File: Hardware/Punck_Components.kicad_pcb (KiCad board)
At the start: 2 copper layers, 91.3 x 100 mm, 109 parts, among them J1 Conn_01x12_Female, J2 Conn_01x12_Female, J3 Conn_01x12_Female, J4 Conn_01x12_Female, J5 SWD_Header, J6 USB_B_Micro, J7 Eurorack_10_pin_power, Q1 MMBT3904, Q2 MMBT3904, Q3 MMBT3904, Q4 MMBT3904, Q5 MMBT3904, Q6 MMBT3904, Q7 MMBT3904, U1 TL072, U2 STM32H743ZITx, U3 W25Q128JVS, U4 PCM5100APW, U5 LM2675M-5, U6 W25Q128JVS, U7 LD1117-3.3-4Tab, Y1 8MHz 20pF

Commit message: Component PCB Signal routing first draft
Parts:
- removed the C31 at (-24.4, 161.0)
- removed the C33 at (-33.0, 166.0)
- removed the C35 at (176.8, 56.9)
- removed the D2 at (168.4, 62.9)
- removed J6: USB_B_Micro, Custom_Footprints:USB_Micro-B_Amphenol
- removed TP10, TP11, TP12, TP9: TestPoint, TestPoint:TestPoint_Pad_2.0x2.0mm
- added C1: 4.7uF, Capacitor_SMD:C_0603_1608Metric_Pad1.08x0.95mm_HandSolder, F.Cu at (121.8, 81.0)
- added C15: 1uF, Capacitor_SMD:C_0603_1608Metric_Pad1.08x0.95mm_HandSolder, F.Cu at (107.8, 81.0)
- added C18: 1uF, Capacitor_SMD:C_0603_1608Metric_Pad1.08x0.95mm_HandSolder, F.Cu at (104.6, 81.0)
- added C19: 100nF, Capacitor_SMD:C_0603_1608Metric_Pad1.08x0.95mm_HandSolder, F.Cu at (106.2, 81.0)
- added C36: 10uF, Resistor_SMD:R_0805_2012Metric, F.Cu at (140.1, 58.0)
- added C37: 10uF, Resistor_SMD:R_0805_2012Metric, F.Cu at (137.7, 58.0)
- added R30: 33k, Resistor_SMD:R_0603_1608Metric_Pad0.98x0.95mm_HandSolder, F.Cu at (150.9, 58.6)
- added R31: 10k, Resistor_SMD:R_0603_1608Metric_Pad0.98x0.95mm_HandSolder, F.Cu at (148.9, 58.6)
- added R5: 100k, Resistor_SMD:R_0603_1608Metric, F.Cu at (130.0, 88.6)
- C34: value 22uF -> 100nF; footprint Capacitor_SMD:C_1210_3225Metric -> Resistor_SMD:R_0805_2012Metric
- C39: footprint Capacitor_SMD:CP_Elec_5x5.8 -> Resistor_SMD:R_1206_3216Metric
- L1: value 68uH -> 3.3uH; footprint Custom_Footprints:TDK_Inductor_6.9x7.2 -> Custom_Footprints:L_0806
- Q1, Q2, Q3, Q4, Q5, Q6, Q7: footprint Package_TO_SOT_THT:TO-92_Inline -> Package_TO_SOT_SMD:SOT-23
- U5: value LM2675M-5 -> TPS561201; footprint Package_SO:SOIC-8_3.9x4.9mm_P1.27mm -> Package_TO_SOT_SMD:SOT-23-6_Handsoldering
- Y1: footprint Crystal:Crystal_SMD_5032-2Pin_5.0x3.2mm_HandSoldering -> Crystal:Crystal_SMD_5032-2Pin_5.0x3.2mm
- moved J4 223.6 mm to (159.0, 112.0)
- moved J3 216.8 mm to (159.0, 56.0)
- moved Q4 197.3 mm to (145.6, 80.6), turned to 180 degrees
- moved R4 196.3 mm to (149.6, 70.6), turned to 180 degrees
- moved R27 195.7 mm to (152.6, 132.3), turned to 180 degrees
- moved J5 189.4 mm to (159.0, 101.8), turned to 90 degrees
- moved R29 188.4 mm to (149.6, 98.8), turned to 180 degrees
- moved Q6 188.2 mm to (145.6, 89.2), turned to 180 degrees
- moved Q2 187.3 mm to (145.6, 71.6), turned to 180 degrees
- moved TP8 186.6 mm to (109.4, 124.4)
- moved R10 185.7 mm to (149.8, 86.0)
- moved R2 184.7 mm to (149.6, 72.8)
- moved R6 183.6 mm to (149.6, 77.2)
- moved C11 182.6 mm to (130.0, 93.0), turned to 180 degrees
- moved Q5 182.0 mm to (145.6, 85.1), turned to 180 degrees
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- renumbered C19 to C20, C1 to C22, C15 to C23, C18 to C24, C20 to C25, C22 to C26, C23 to C27, C24 to C28, C25 to C29, C26 to C30, C27 to C31, C28 to C32, C29 to C33, C30 to C35, C32 to C38, C36 to C40, C37 to C41, C38 to C42, C40 to C44, D3 to D2, R17 to R10, R18 to R11, R3 to R12, R6 to R13, R7 to R14, R19 to R15, R8 to R16, R20 to R17, R21 to R18, R22 to R19, R11 to R20, R23 to R21, R14 to R22, R15 to R23, R16 to R25, R25 to R26, R26 to R27, R27 to R28, R28 to R29, R4 to R3, R5 to R4, R9 to R6, R10 to R7, R12 to R8, R13 to R9
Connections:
- C34 pad 1: VCC -> /VSW
- C34 pad 2: GND -> /CB
- J1 pad 1: +3.3VA -> GND
- J1 pad 10: /SA_LED -> /SAMPLER_A_VOL_POT
- J1 pad 11: /SNARE_IN -> /SAMPLER_B_VOICE_POT
- J1 pad 12: GND -> /HIHAT_DECAY_POT
- J1 pad 2: /KICK_IN -> /SAMPLER_A_VOICE_POT
- J1 pad 3: /SN_BTN -> /SAMPLER_A_SPEED_POT
- J1 pad 4: /SN_LED -> /KICK_ATTACK_POT
- J1 pad 5: /OH_BTN -> /KICK_DECAY_POT
- J1 pad 6: /OH_LED -> /KICK_VOL_POT
- J1 pad 7: /CH_BTN -> /SNARE_FILTER_POT
- J1 pad 8: /CH_LED -> /SNARE_TUNING_POT
- J1 pad 9: /SA_BTN -> /SNARE_VOL_POT
- J2 pad 1: /KI_BTN -> /HIHAT_VOL_POT
- J2 pad 10: /SNARE_TUNING_POT -> /CH_BTN
- J2 pad 11: /SNARE_VOL_POT -> /KI_BTN
- J2 pad 2: /KI_LED -> /SAMPLER_B_SPEED_POT
- J2 pad 3: /CH_IN -> /SAMPLER_B_VOL_POT
- J2 pad 4: /SB_BTN -> /TEMPO_POT
- J2 pad 5: /SB_LED -> /MIDI_LEARN
- J2 pad 6: /KICK_ATTACK_POT -> /SEQ_SELECT
- J2 pad 7: /KICK_DECAY_POT -> /SA_BTN
- J2 pad 8: /KICK_VOL_POT -> /SB_BTN
- J2 pad 9: /SNARE_FILTER_POT -> /SN_BTN
- J3 pad 1: /OH_IN -> GND
- J3 pad 10: /SAMPLER_B_VOL_POT -> /SA_LED
- J3 pad 11: /TEMPO_OUT -> /SB_LED
- J3 pad 12: GND -> +3.3VA
- J3 pad 2: /SAMPLERA_IN -> /KICK_IN
- J3 pad 3: /HIHAT_DECAY_POT -> /SAMPLER_A_IN
- J3 pad 4: /HIHAT_VOL_POT -> /SNARE_IN
- J3 pad 5: /SAMPLER_A_VOICE_POT -> /SAMPLER_B_IN
- J3 pad 6: /SAMPLER_A_SPEED_POT -> /CH_IN
- J3 pad 7: /SAMPLER_A_VOL_POT -> /MIDI_IN
- J3 pad 8: /SAMPLER_B_VOICE_POT -> /OH_IN
- J3 pad 9: /SAMPLER_B_SPEED_POT -> /TEMPO_OUT
- J4 pad 1: +3.3VA -> GND
- J4 pad 10: /AUDIO_OUT_R -> /AUDIO_OUT_L
- J4 pad 11: /AUDIO_OUT_L -> /AUDIO_OUT_R
- J4 pad 12: GND -> +3.3VA
- J4 pad 2: /SAMPLERB_IN -> /OH_BTN
- J4 pad 6: /MIDI_IN -> /KI_LED
- J4 pad 7: /MIDI_LEARN -> /SN_LED
- J4 pad 8: /SEQ_SELECT -> /CH_LED
- J4 pad 9: /TEMPO_POT -> /OH_LED
- L1 pad 2: +5V -> +3V3
- L2 pad 2: +3V3 -> /VO
- Q6 pad 3: /MIDI_RX -> /MIDI_CLAMP
- R15 pad 1: /MIDI_RX -> /MIDI_CLAMP
- U2 pad 1: /QSPI_IO2 -> /QSPI_BK1_IO2
- U2 pad 10: /KI_BTN -> unconnected-(U2-Pad10)
- U2 pad 11: /SN_BTN -> unconnected-(U2-Pad11)
- U2 pad 114: unconnected-(U2-Pad114) -> /OH_BTN
- U2 pad 12: /OH_BTN -> unconnected-(U2-Pad12)
- U2 pad 124: unconnected-(U2-Pad124) -> /OH_CLAMP
- U2 pad 125: /SAMPLER_A_CLAMP -> /MIDI_CLAMP
- U2 pad 128: /SAMPLER_B_CLAMP -> /CH_CLAMP
- U2 pad 13: /CH_BTN -> unconnected-(U2-Pad13)
- U2 pad 135: /SNARE_CLAMP -> /SAMPLER_B_CLAMP
- U2 pad 136: /CH_CLAMP -> /SNARE_CLAMP
- U2 pad 137: /KICK_CLAMP -> /SAMPLER_A_CLAMP
- U2 pad 138: GND -> Net-(R5-Pad2)
- U2 pad 14: /SA_BTN -> unconnected-(U2-Pad14)
- U2 pad 140: /DAC_LRCLK -> unconnected-(U2-Pad140)
- U2 pad 141: /MIDI_RX -> /KICK_CLAMP
- U2 pad 15: /SB_BTN -> unconnected-(U2-Pad15)
- U2 pad 64: unconnected-(U2-Pad64) -> /MIDI_LEARN
- U2 pad 65: unconnected-(U2-Pad65) -> /SEQ_SELECT
- U2 pad 66: unconnected-(U2-Pad66) -> /SA_BTN
- U2 pad 67: /MIDI_LEARN -> /SB_BTN
- U2 pad 68: /SEQ_SELECT -> /SN_BTN
- U2 pad 69: unconnected-(U2-Pad69) -> /CH_BTN
- U2 pad 73: unconnected-(U2-Pad73) -> /DAC_LRCLK
- U2 pad 78: unconnected-(U2-Pad78) -> /KI_BTN
- U2 pad 93: /OH_CLAMP -> unconnected-(U2-Pad93)
- U2 pad 96: /KI_LED_OUT -> /OH_LED_OUT
- U2 pad 97: /SN_LED_OUT -> /CH_LED_OUT
- U2 pad 98: /CH_LED_OUT -> /SN_LED_OUT
- U2 pad 99: /OH_LED_OUT -> /KI_LED_OUT
- U5 pad 1: Net-(C31-Pad2) -> GND
- U5 pad 2: unconnected-(U5-Pad2) -> /VSW
- U5 pad 3: unconnected-(U5-Pad3) -> VCC
- U5 pad 4: +5V -> /FB
- U5 pad 5: unconnected-(U5-Pad5) -> VCC
- U5 pad 6: GND -> /CB
- U7 pad 2: +3V3 -> /VO
- U7 pad 3: +5V -> VCC
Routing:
- net +3V3: track 0.00 -> 70.9 mm
- net VCC: track 0.00 -> 67.8 mm
- net /KI_BTN: track 0.00 -> 52.1 mm
- net /SAMPLER_A_VOICE_POT: track 0.00 -> 51.4 mm, vias 0 -> 1
- net /QSPI_CLK: track 0.00 -> 51.1 mm, vias 0 -> 2
- net /SAMPLER_A_SPEED_POT: track 0.00 -> 49.5 mm, vias 0 -> 1
- net /SAMPLER_B_VOL_POT: track 0.00 -> 49.4 mm, vias 0 -> 2
- net /CH_BTN: track 0.00 -> 48.6 mm
- net /SAMPLER_B_SPEED_POT: track 0.00 -> 48.2 mm, vias 0 -> 2
- net /OH_LED_OUT: track 0.00 -> 47.2 mm
- net /SN_BTN: track 0.00 -> 46.7 mm
- net /CH_LED_OUT: track 0.00 -> 45.3 mm
- net /KICK_ATTACK_POT: track 0.00 -> 45.1 mm
- net /HIHAT_VOL_POT: track 0.00 -> 45.0 mm
- net /USB_VBUS: track 0.00 -> 45.0 mm
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- added copper zone on In1.Cu, net /VSW
- added copper zone on B.Cu, net GND
- added copper zone on F.Cu, net GND
- added copper zone on In2.Cu, net GND
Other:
- board size 91.3 x 100 mm -> 91.2 x 99.8 mm
- copper layers 2 -> 4

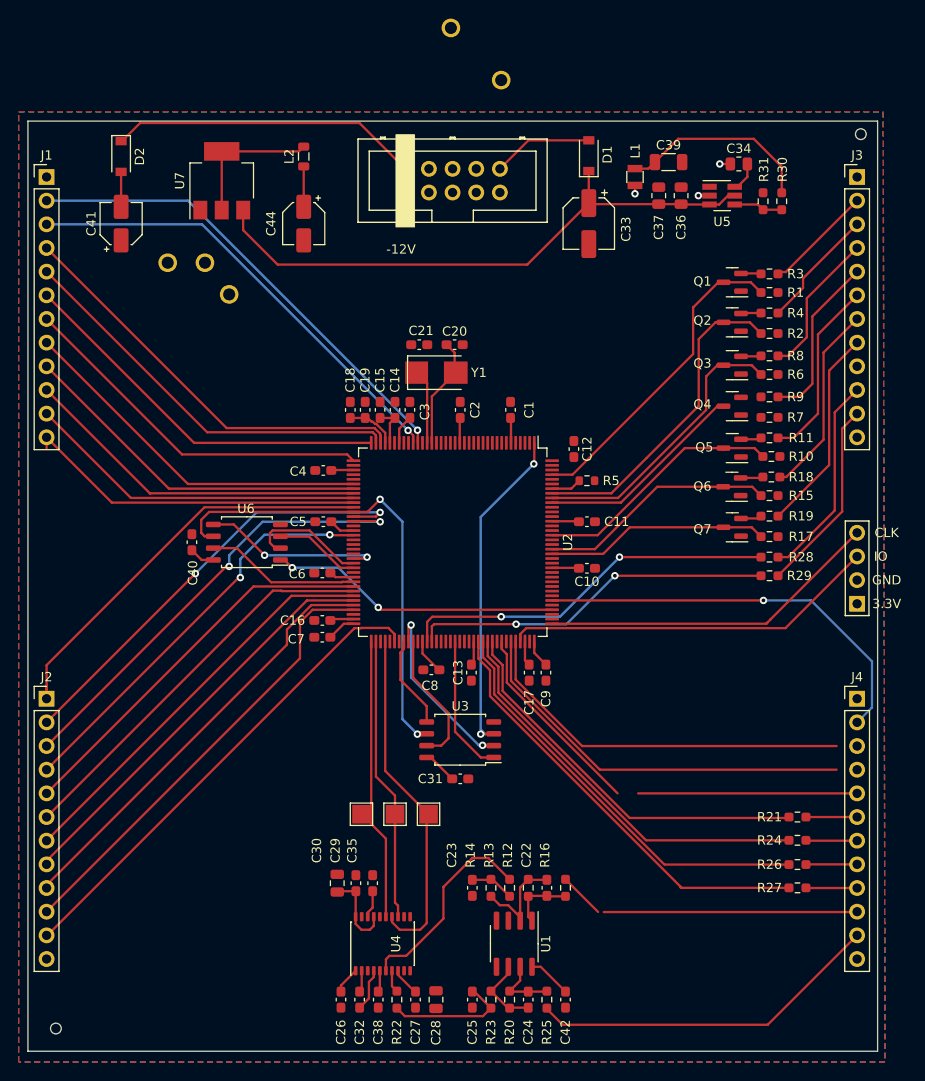
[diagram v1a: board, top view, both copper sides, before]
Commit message: Power routing on component PCB
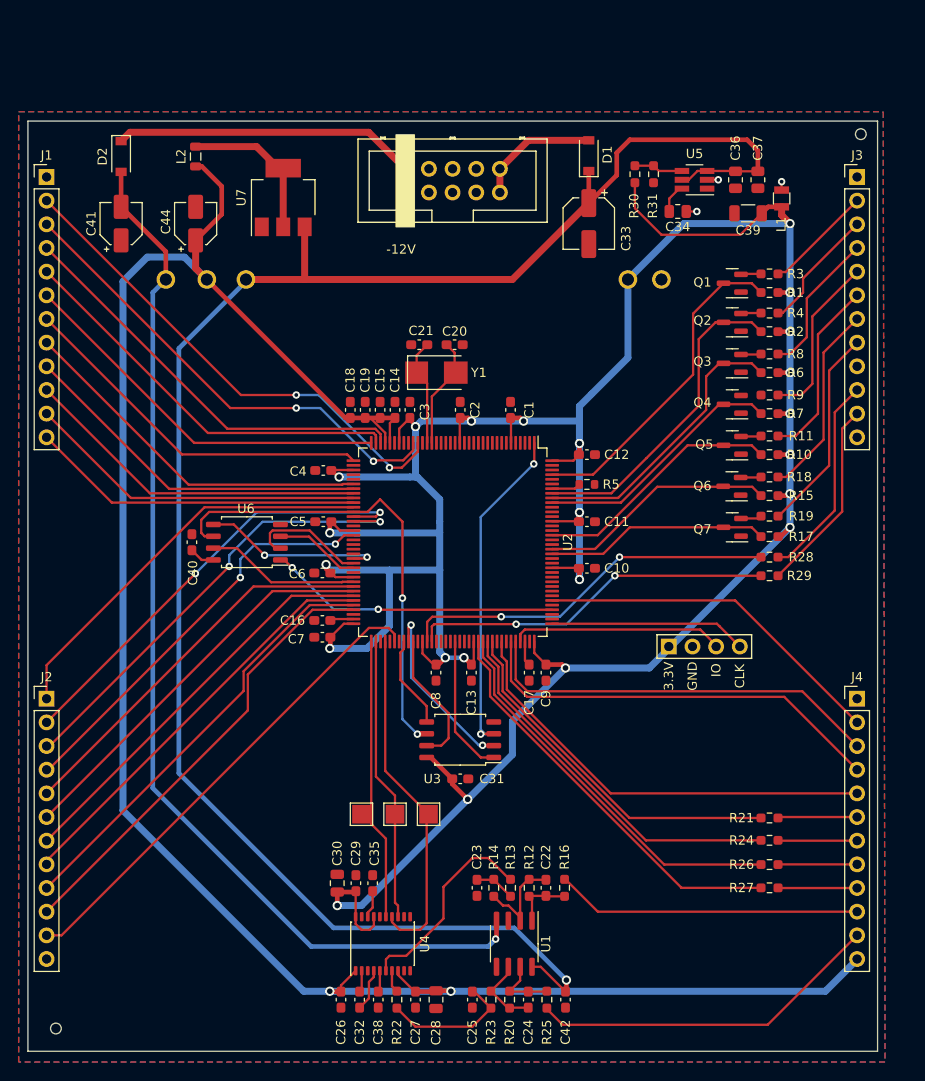
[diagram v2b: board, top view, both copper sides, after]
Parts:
- moved TP1 35.2 mm to (138.0, 67.0)
- moved TP2 25.4 mm to (134.4, 67.0)
- moved J5 20.7 mm to (138.8, 106.4), turned to 0 degrees
- moved R30 16.0 mm to (135.2, 55.7), turned to 90 degrees
- moved L1 15.9 mm to (150.9, 58.3), turned to -90 degrees
- moved R31 12.1 mm to (137.2, 55.7), turned to -90 degrees
- moved C44 11.6 mm to (88.0, 61.0), turned to 90 degrees
- moved L2 11.6 mm to (88.0, 53.8)
- moved C37 10.8 mm to (148.3, 56.3), turned to -90 degrees
- moved C39 10.2 mm to (147.3, 59.9), turned to 180 degrees
- moved C34 8.31 mm to (139.8, 59.7), turned to 180 degrees
- moved U7 6.84 mm to (97.4, 58.2)
- moved C36 6.08 mm to (145.9, 56.3), turned to -90 degrees
- moved TP4 4.75 mm to (93.4, 67.0)
- moved U5 3.41 mm to (141.6, 56.3), turned to 180 degrees
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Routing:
- net +3V3: track 70.9 -> 358.7 mm, vias 0 -> 23
- net +3.3VA: track 20.5 -> 215.1 mm, vias 0 -> 2
- net VCC: track 67.8 -> 196.3 mm, vias 0 -> 1
- net VEE: track 3.75 -> 114.9 mm, vias 0 -> 1
- net /SWIO: track 40.4 -> 22.9 mm
- net /SWCLK: track 37.0 -> 21.2 mm
- net /OH_BTN: track 44.6 -> 38.2 mm, vias 1 -> 0
- net /SAMPLER_B_CLAMP: track 22.7 -> 27.2 mm
- net Net-(C21-Pad1): track 8.00 -> 11.5 mm
- net /OH_LED_OUT: track 47.2 -> 44.1 mm
- net /KI_LED: track 5.49 -> 8.53 mm
- net /KI_LED_OUT: track 42.2 -> 39.1 mm
- net /CH_LED: track 5.50 -> 8.50 mm
- net /SN_LED: track 5.50 -> 8.50 mm
- net /OH_LED: track 5.50 -> 8.50 mm
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
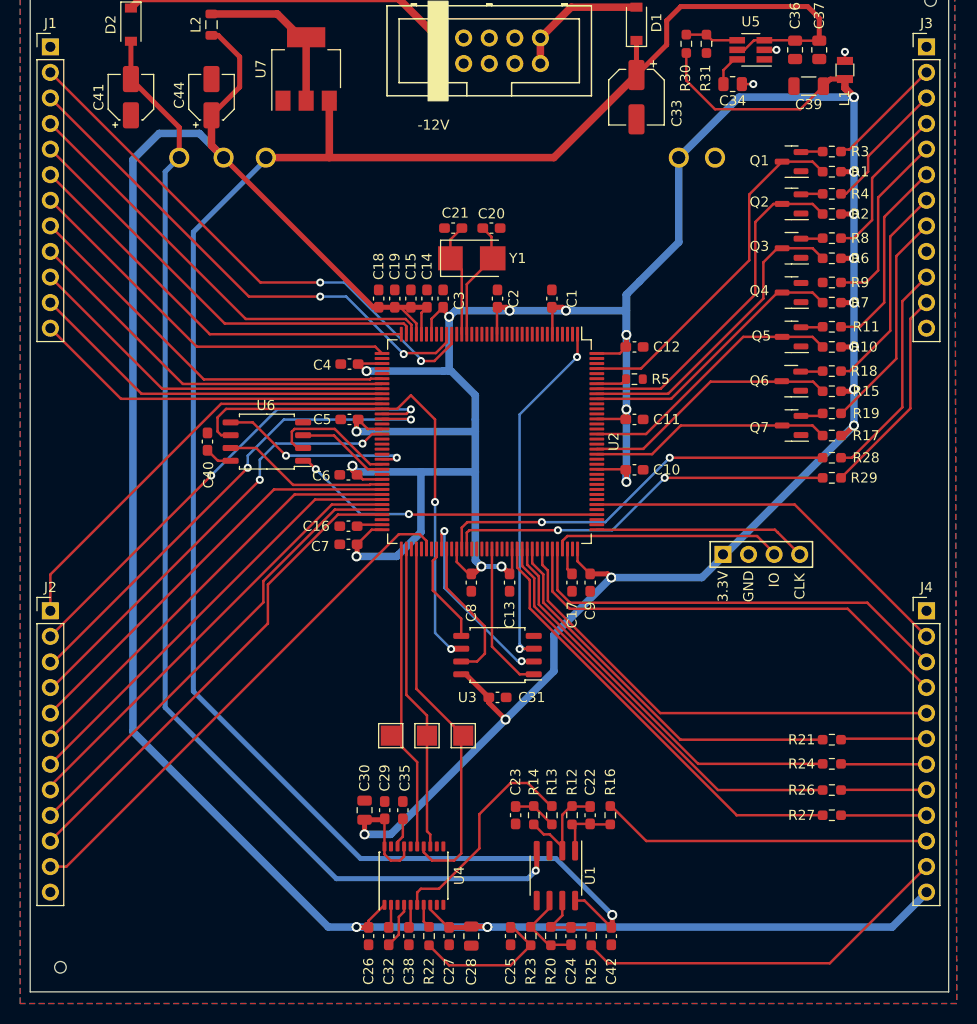
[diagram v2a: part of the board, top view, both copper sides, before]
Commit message: More component routing
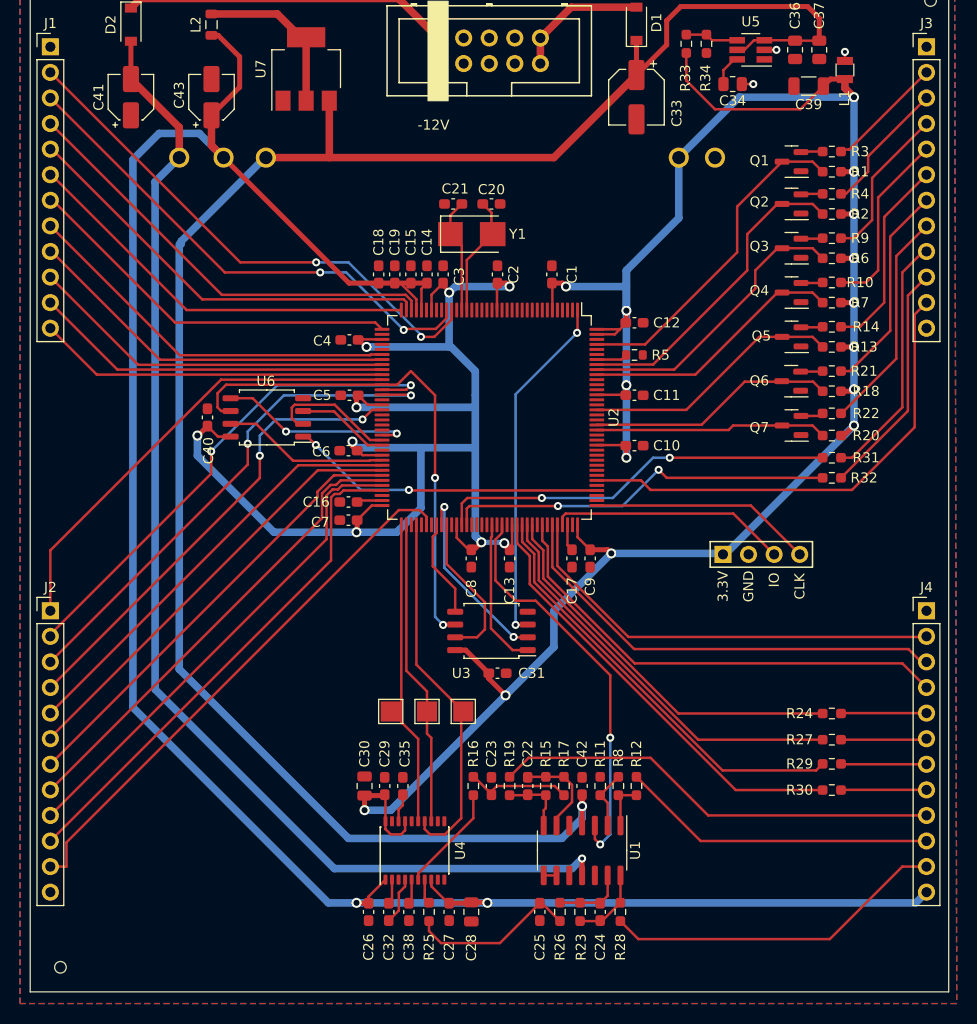
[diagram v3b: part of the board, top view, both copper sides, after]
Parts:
- added R11: 10k, Resistor_SMD:R_0603_1608Metric_Pad0.98x0.95mm_HandSolder, F.Cu at (126.6, 129.4)
- added R12: 1k, Resistor_SMD:R_0603_1608Metric_Pad0.98x0.95mm_HandSolder, F.Cu at (130.2, 129.4)
- added R8: 15k, Resistor_SMD:R_0603_1608Metric_Pad0.98x0.95mm_HandSolder, F.Cu at (128.4, 129.4)
- U1: value TL072 -> TL074; footprint Package_SO:SOIC-8_3.9x4.9mm_P1.27mm -> Package_SO:SOIC-14_3.9x8.7mm_P1.27mm
- moved C42 15.2 mm to (124.8, 129.4), turned to 90 degrees
- moved R19 10.4 mm to (117.6, 129.4)
- moved R16 8.32 mm to (114.0, 129.4), turned to -90 degrees
- moved C22 6.84 mm to (119.4, 129.4)
- moved R17 4.17 mm to (123.0, 129.4), turned to -90 degrees
- moved R15 3.89 mm to (121.2, 129.4)
- moved C23 3.76 mm to (115.8, 129.4), turned to 90 degrees
- moved C24 3.76 mm to (126.6, 141.9), turned to 90 degrees
- moved C25 3.76 mm to (120.6, 141.9)
- moved R23 3.76 mm to (124.6, 141.9), turned to 90 degrees
- moved R26 3.76 mm to (122.6, 141.9)
- moved R28 3.76 mm to (128.6, 141.9)
- moved U1 3.61 mm to (124.8, 135.8)
- moved R29 2.60 mm to (149.6, 127.2)
- moved R24 2.60 mm to (149.6, 122.2)
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- renumbered C44 to C43, J7 to J6, R9 to R10, R10 to R13, R11 to R14, R12 to R15, R13 to R16, R14 to R17, R15 to R18, R16 to R19, R17 to R20, R18 to R21, R19 to R22, R20 to R23, R21 to R24, R22 to R25, R23 to R26, R24 to R27, R25 to R28, R26 to R29, R27 to R30, R28 to R31, R29 to R32, R30 to R33, R31 to R34, R8 to R9
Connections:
- J3 pad 10: /SA_LED -> /SB_LED
- J3 pad 11: /SB_LED -> /OH_BTN
- J3 pad 12: +3.3VA -> unconnected-(J3-Pad12)
- J3 pad 9: /TEMPO_OUT -> /SA_LED
- J4 pad 10: /AUDIO_OUT_L -> /TEMPO_OUT
- J4 pad 2: /OH_BTN -> /USB_DP
- J4 pad 3: /USB_DP -> /USB_DM
- J4 pad 4: /USB_DM -> /USB_VBUS
- J4 pad 5: /USB_VBUS -> /KI_LED
- J4 pad 6: /KI_LED -> /SN_LED
- J4 pad 7: /SN_LED -> /CH_LED
- J4 pad 8: /CH_LED -> /OH_LED
- J4 pad 9: /OH_LED -> /AUDIO_OUT_L
- U1 pad 1: Net-(C22-Pad1) -> Net-(R12-Pad1)
- U1 pad 2: Net-(C22-Pad2) -> Net-(R11-Pad1)
- U1 pad 3: GND -> /TEMPO_CLOCK
- U1 pad 4: VEE -> VCC
- U1 pad 6: Net-(C24-Pad2) -> Net-(C22-Pad2)
- U1 pad 7: Net-(C24-Pad1) -> Net-(C22-Pad1)
- U1 pad 8: VCC -> Net-(U1-Pad8)
- U2 pad 134: /TEMPO_OUT -> unconnected-(U2-Pad134)
- U2 pad 93: unconnected-(U2-Pad93) -> /TEMPO_CLOCK
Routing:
- net /TEMPO_CLOCK: track 0.00 -> 40.4 mm, vias 0 -> 2
- net /TEMPO_OUT: track 0.00 -> 31.4 mm
- net +3V3: track 358.7 -> 373.7 mm, vias 23 -> 24
- net /AUDIO_OUT_L: track 32.8 -> 44.6 mm
- net /DAC_OUT_L: track 22.0 -> 10.7 mm
- net /OH_BTN: track 38.2 -> 47.4 mm
- net Net-(C23-Pad1): track 4.02 -> 10.7 mm
- net Net-(R11-Pad1): track 0.00 -> 5.89 mm
- net VCC: track 196.3 -> 190.7 mm
- net Net-(R12-Pad1): track 0.00 -> 4.90 mm
- net VEE: track 114.9 -> 119.2 mm
- net +3.3VA: track 215.1 -> 210.9 mm
- net /AUDIO_OUT_R: track 38.1 -> 34.1 mm
- net /SAMPLER_A_CLAMP: track 34.6 -> 31.6 mm
- net /SA_LED: track 22.1 -> 24.8 mm
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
